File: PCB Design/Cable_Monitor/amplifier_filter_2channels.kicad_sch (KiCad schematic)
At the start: 6 parts, among them U2 MCP6002-xSN

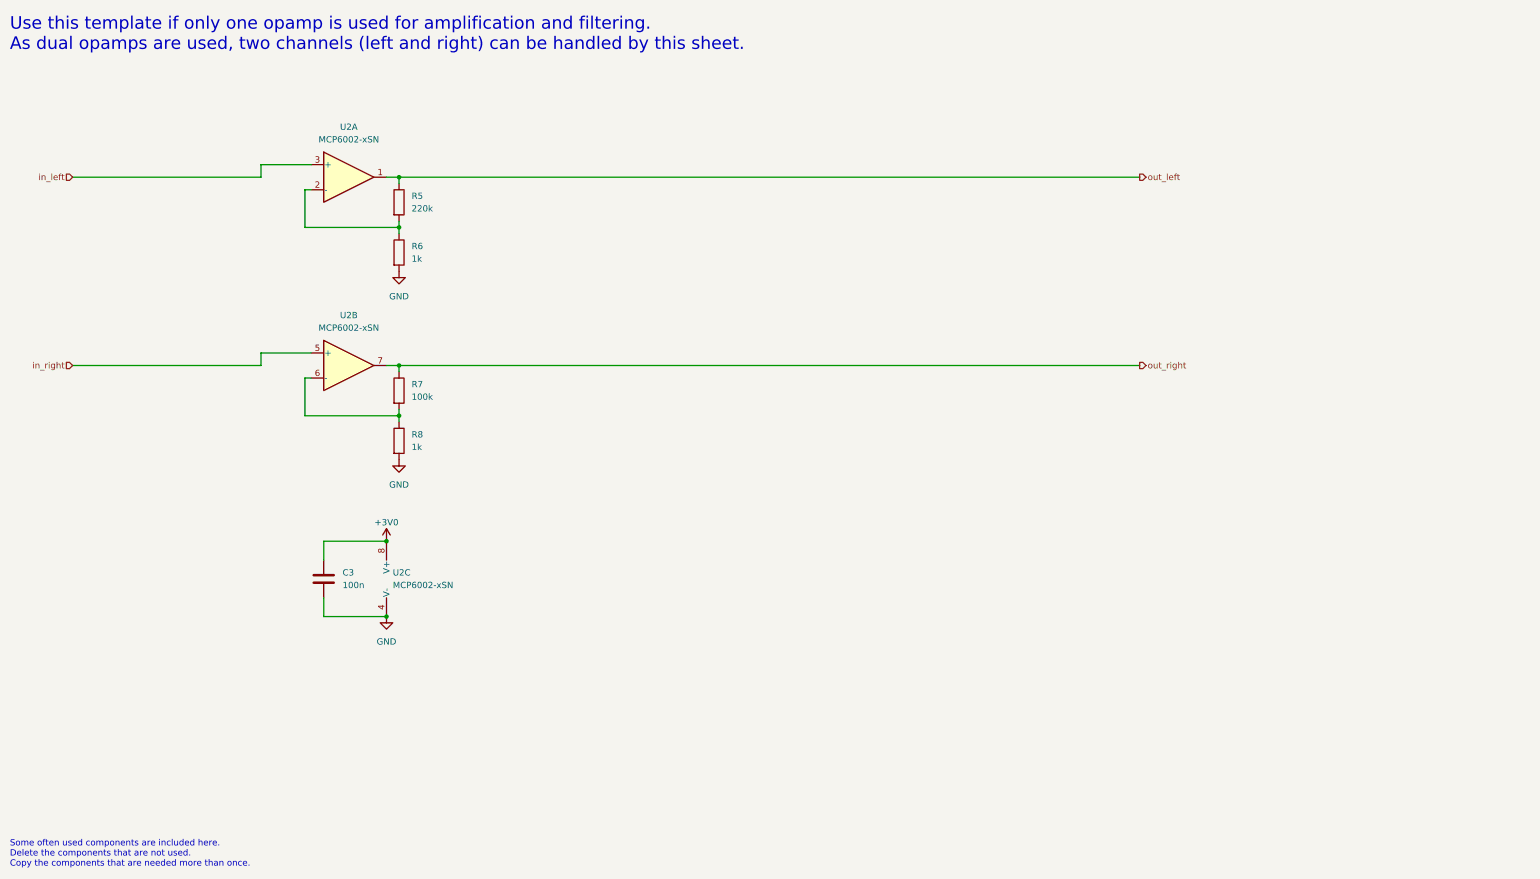
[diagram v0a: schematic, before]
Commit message: Modified Schematics
Added Virtual GND and adapted the Pads Left and Right
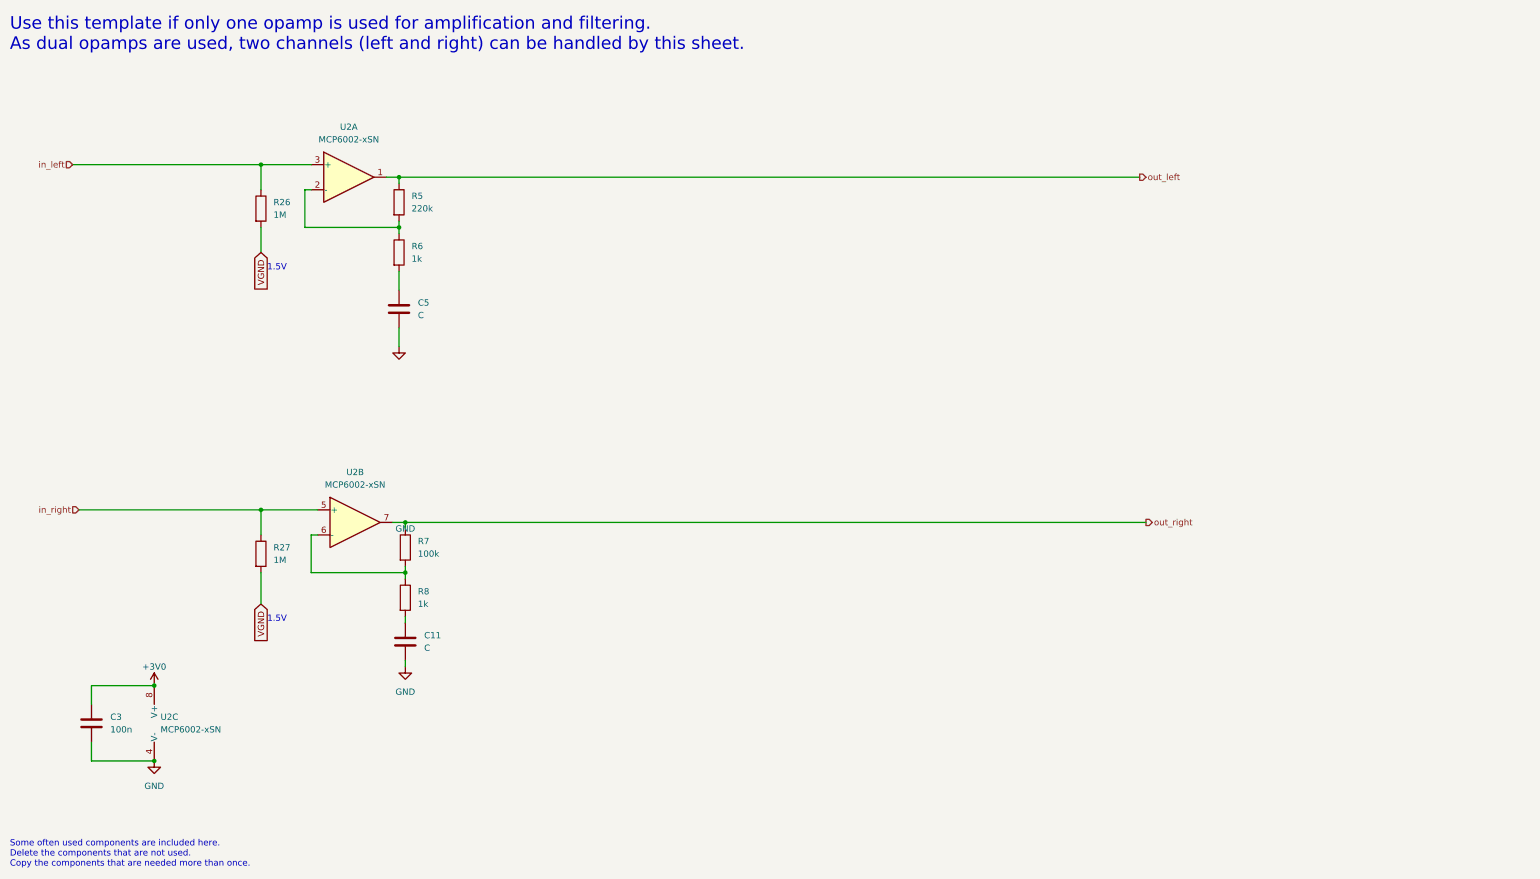
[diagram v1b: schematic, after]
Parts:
- added C11, C5: C, symbol Device:C
- added R26: 1M, Resistor_SMD:R_0805_2012Metric_Pad1.20x1.40mm_HandSolder, symbol Device:R
- added R27: 1M, symbol Device:R
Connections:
- net GND: now also C11.2, C5.2; no longer R6.2, R8.2
- net in_left: now also R26.1
- net in_right: now also R27.1
- new net: C11.1, R8.2
- new net: C5.1, R6.2
- new net VGND: R26.2, R27.2
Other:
- note added: "1.5V"
- moved on the sheet: C3, R7, R8, U2B, U2C

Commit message: PCB Layout Update
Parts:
- added C10, C11, C12, C13, C14, C15: C, symbol Device:C
- added C20: 100n, Capacitor_SMD:C_0805_2012Metric_Pad1.18x1.45mm_HandSolder, symbol Device:C
- added R10, R11, R12, R13, R14, R9: R, symbol Device:R
- added U3: MCP6002-xSN, Package_SO:SOIC-8_3.9x4.9mm_P1.27mm, symbol Amplifier_Operational:MCP6002-xSN
- renumbered C3 to C7, C5 to C8, C11 to C9, R26 to R3, R27 to R4, U2 to U4
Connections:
- net +3V0: now also C20.1, U3.4 (V-)
- net GND: now also C20.2, R11.2, R12.2, U3.8 (V+)
- net VGND: now also U3.3 (+), U3.5 (+)
- net out_left: now also C12.2, R13.1, U3.1; no longer R5.1, U4.1
- net out_right: now also C14.2, R14.1, U3.7; no longer R7.1, U4.7
- new net: C11.2, R10.1
- new net: C14.1, C15.1, R10.2, R12.1
- new net: C12.1, C13.1, R11.1, R9.2
- new net: C13.2, R13.2, U3.2 (-)
- new net: C11.1, R7.1, U4.7
- new net: C10.1, R5.1, U4.1
- new net: C15.2, R14.2, U3.6 (-)
- new net: C10.2, R9.1
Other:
- note added: "Supply Voltage for OPAmps"
- moved on the sheet: C7, C9, R4, R7, R8, U4B, U4C

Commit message: PCB Design Update
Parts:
- removed C10, C11, C8, C9: C, symbol Device:C
- removed R5: 220k, Resistor_SMD:R_0805_2012Metric_Pad1.20x1.40mm_HandSolder, symbol Device:R
- removed R7: 100k, Resistor_SMD:R_0805_2012Metric_Pad1.20x1.40mm_HandSolder, symbol Device:R
- removed R8: 1k, Resistor_SMD:R_0805_2012Metric_Pad1.20x1.40mm_HandSolder, symbol Device:R
- removed R9: R, symbol Device:R
- C11: renamed from C12; value C -> 18nF
- C12: renamed from C13; value C -> 330nF
- C13: renamed from C14; value C -> 18nF
- C14: renamed from C15; value C -> 330nF
- R10: renamed from R14; value R -> 560k
- R5: renamed from R10; value R -> 5.1k
- R6: value 1k -> 5.1k; footprint Resistor_SMD:R_0805_2012Metric_Pad1.20x1.40mm_HandSolder -> (none)
- R7: renamed from R11; value R -> 7.5k
- R8: renamed from R12; value R -> 7.5k
- R9: renamed from R13; value R -> 560k
- renumbered C20 to C10, C7 to C9, R4 to R3, R3 to R4, U4 to U5, U3 to U5, U3 to U6, U4 to U6
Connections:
- net VGND: now also U5.5 (+); no longer U5.3 (+)
- net in_right: now also U6.3 (+); no longer U6.5 (+)
- net out_left: now also U5.7; no longer U5.1
- net at R5.1: now also U6.1, U6.2 (-)
- net at C11.1, C12.1, R7.1: now also R6.2
- net at C12.2, R9.2: now also U5.6 (-); no longer U5.2 (-)
- net at U5.1: now also R6.1, U5.2 (-)
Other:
- moved on the sheet: R3, R4, R5

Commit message: Letzte Anpassungen am Schema
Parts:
- added TP4: pad_right_sf, TestPoint:TestPoint_Loop_D2.60mm_Drill1.6mm_Beaded, symbol Connector:TestPoint
- added TP4: pad_left_sf, TestPoint:TestPoint_Loop_D2.60mm_Drill1.6mm_Beaded, symbol Connector:TestPoint
- renumbered R7 to R10, R8 to R11, R9 to R12, R10 to R13, R3 to R6, R4 to R7, R5 to R8, R6 to R9
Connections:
- net at R8.1, U6.1, U6.2 (-): now also TP4.1
- net at R9.1, U5.1, U5.2 (-): now also TP4.1

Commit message: Schema Updates, bald Fertig
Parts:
- C11, C12, C13, C14: footprint (none) -> Capacitor_SMD:C_0805_2012Metric_Pad1.18x1.45mm_HandSolder
- R10, R11, R12, R13, R6, R8, R9: footprint (none) -> Resistor_SMD:R_0805_2012Metric_Pad1.20x1.40mm_HandSolder
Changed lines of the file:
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@@
       (effects (font (size 1.27 1.27)))
     )
-    (property "Footprint" "" (at 121.92 103.378 90)
+    (property "Footprint" "Resistor_SMD:R_0805_2012Metric_Pad1.20x1.40mm_HandSolder" (at 121.92 103.378 90)
       (effects (font (size 1.27 1.27)) hide)
     )
@@
       (effects (font (size 1.27 1.27)))
     )
-    (property "Footprint" "" (at 158.75 49.8348 0)
+    (property "Footprint" "Capacitor_SMD:C_0805_2012Metric_Pad1.18x1.45mm_HandSolder" (at 158.75 49.8348 0)
       (effects (font (size 1.27 1.27)) hide)
     )
@@
       (effects (font (size 1.27 1.27)) (justify left))
     )
-    (property "Footprint" "" (at 141.732 106.68 90)
+    (property "Footprint" "Resistor_SMD:R_0805_2012Metric_Pad1.20x1.40mm_HandSolder" (at 141.732 106.68 90)
       (effects (font (size 1.27 1.27)) hide)
     )
@@
       (effects (font (size 1.27 1.27)))
     )
-    (property "Footprint" "" (at 158.75 100.6348 0)
+    (property "Footprint" "Capacitor_SMD:C_0805_2012Metric_Pad1.18x1.45mm_HandSolder" (at 158.75 100.6348 0)
       (effects (font (size 1.27 1.27)) hide)
     )
@@
         )
         (path "/1f276d59-ad9b-4e70-a842-f3b7e562eb9b/12fcc65d-dd77-40b1-ae40-e29cdf7d08dc"
-          (reference "TP13") (unit 1)
+          (reference "TP20") (unit 1)
         )
       )
@@
       (effects (font (size 1.27 1.27)) (justify left))
     )
-    (property "Footprint" "" (at 160.782 95.25 90)
+    (property "Footprint" "Resistor_SMD:R_0805_2012Metric_Pad1.20x1.40mm_HandSolder" (at 160.782 95.25 90)
       (effects (font (size 1.27 1.27)) hide)
     )
@@
       (effects (font (size 1.27 1.27)) (justify left))
     )
-    (property "Footprint" "" (at 160.782 44.45 90)
+    (property "Footprint" "Resistor_SMD:R_0805_2012Metric_Pad1.20x1.40mm_HandSolder" (at 160.782 44.45 90)
       (effects (font (size 1.27 1.27)) hide)
     )
@@
       (effects (font (size 1.27 1.27)))
     )
-    (property "Footprint" "" (at 158.75 89.2048 0)
+    (property "Footprint" "Capacitor_SMD:C_0805_2012Metric_Pad1.18x1.45mm_HandSolder" (at 158.75 89.2048 0)
       (effects (font (size 1.27 1.27)) hide)
     )
@@
       (effects (font (size 1.27 1.27)))
     )
-    (property "Footprint" "" (at 123.19 52.578 90)
+    (property "Footprint" "Resistor_SMD:R_0805_2012Metric_Pad1.20x1.40mm_HandSolder" (at 123.19 52.578 90)
       (effects (font (size 1.27 1.27)) hide)
     )
@@
       (effects (font (size 1.27 1.27)) (justify left))
     )
-    (property "Footprint" "" (at 141.732 55.88 90)
+    (property "Footprint" "Resistor_SMD:R_0805_2012Metric_Pad1.20x1.40mm_HandSolder" (at 141.732 55.88 90)
       (effects (font (size 1.27 1.27)) hide)
     )
@@
       (effects (font (size 1.27 1.27)) (justify left))
     )
-    (property "Footprint" "" (at 73.152 113.03 90)
+    (property "Footprint" "Resistor_SMD:R_0805_2012Metric_Pad1.20x1.40mm_HandSolder" (at 73.152 113.03 90)
       (effects (font (size 1.27 1.27)) hide)
     )
@@
       (effects (font (size 1.27 1.27)))
     )
-    (property "Footprint" "" (at 158.75 38.4048 0)
+    (property "Footprint" "Capacitor_SMD:C_0805_2012Metric_Pad1.18x1.45mm_HandSolder" (at 158.75 38.4048 0)
       (effects (font (size 1.27 1.27)) hide)
     )
@@
         )
         (path "/1f276d59-ad9b-4e70-a842-f3b7e562eb9b/12fcc65d-dd77-40b1-ae40-e29cdf7d08dc"
-          (reference "TP12") (unit 1)
-        )
-      )
+          (reference "TP19") (unit 1)
+        )
+      )

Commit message: Update
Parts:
- renumbered R7 to R10, R8 to R11, R9 to R12, R10 to R13, R11 to R14, R12 to R15, R13 to R16, R6 to R9
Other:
- note added: "Filtering and Amplification to measure Electric Fields. This will allow us to measure Fields generated by Cables and thus allow us to calculate the distance from an AC Voltage source."
- note removed: "Some often used components are included here. Delete the components that are not used. Copy the components that are needed more than once."
- note removed: "Use this template if only one opamp is used for amplification and filtering. As dual opamps are used, two channels (left and right) can be handled by this sheet."
- company: hhrt@zhaw.ch -> ZHAW
- title: Amplifiers and Filters -> Amplifiers and Filters for Pads

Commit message: Almost Donezo
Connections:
- net +3V0: now also U6.8 (V+); no longer U6.4 (V-)
- net GND: now also U6.4 (V-); no longer U6.8 (V+)
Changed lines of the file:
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@@
     )
   )
-  (symbol (lib_id "Amplifier_Operational:MCP6002-xSN") (at 76.2 167.64 0) (mirror x) (unit 3)
+  (symbol (lib_id "Amplifier_Operational:MCP6002-xSN") (at 76.2 167.64 0) (unit 3)
     (in_bom yes) (on_board yes) (dnp no)
-    (property "Reference" "U6" (at 77.47 166.37 0)
+    (property "Reference" "U6" (at 77.47 168.91 0)
       (effects (font (size 1.27 1.27)))
     )
-    (property "Value" "MCP6002-xSN" (at 82.55 168.91 0)
+    (property "Value" "MCP6002-xSN" (at 82.55 166.37 0)
       (effects (font (size 1.27 1.27)))
     )
@@
       (effects (font (size 1.27 1.27)) hide)
     )
-    (property "Sim.Pins" "1=1out 2=1in- 3=1in+ 4=vcc- 5=2in+ 6=2in- 7=2out 8=vcc+" (at -17.78 218.44 0)
+    (property "Sim.Pins" "1=1out 2=1in- 3=1in+ 4=vcc- 5=2in+ 6=2in- 7=2out 8=vcc+" (at -17.78 116.84 0)
       (effects (font (size 1.27 1.27)) hide)
     )

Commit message: Updated Schematics
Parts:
- renumbered C9 to C10, C10 to C11, C11 to C12, C12 to C13, C13 to C14, C14 to C15
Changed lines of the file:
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@@
   (symbol (lib_id "Device:C") (at 154.94 50.8 90) (unit 1)
     (in_bom yes) (on_board yes) (dnp no)
-    (property "Reference" "C12" (at 154.94 54.61 90)
+    (property "Reference" "C13" (at 154.94 54.61 90)
       (effects (font (size 1.27 1.27)))
     )
@@
       (project "Cable_Monitor"
         (path "/1f276d59-ad9b-4e70-a842-f3b7e562eb9b/12fcc65d-dd77-40b1-ae40-e29cdf7d08dc"
-          (reference "C12") (unit 1)
+          (reference "C13") (unit 1)
         )
       )
@@
   (symbol (lib_id "power:GND") (at 73.66 175.26 0) (unit 1)
     (in_bom yes) (on_board yes) (dnp no) (fields_autoplaced)
-    (property "Reference" "#PWR039" (at 73.66 181.61 0)
+    (property "Reference" "#PWR040" (at 73.66 181.61 0)
       (effects (font (size 1.27 1.27)) hide)
     )
@@
       (project "Cable_Monitor"
         (path "/1f276d59-ad9b-4e70-a842-f3b7e562eb9b/12fcc65d-dd77-40b1-ae40-e29cdf7d08dc"
-          (reference "#PWR039") (unit 1)
+          (reference "#PWR040") (unit 1)
         )
       )
@@
   (symbol (lib_id "power:GND") (at 40.64 175.26 0) (unit 1)
     (in_bom yes) (on_board yes) (dnp no) (fields_autoplaced)
-    (property "Reference" "#PWR037" (at 40.64 181.61 0)
+    (property "Reference" "#PWR038" (at 40.64 181.61 0)
       (effects (font (size 1.27 1.27)) hide)
     )
@@
       (project "Cable_Monitor"
         (path "/1f276d59-ad9b-4e70-a842-f3b7e562eb9b/12fcc65d-dd77-40b1-ae40-e29cdf7d08dc"
-          (reference "#PWR037") (unit 1)
+          (reference "#PWR038") (unit 1)
         )
       )
@@
   (symbol (lib_id "Device:C") (at 60.96 167.64 0) (unit 1)
     (in_bom yes) (on_board yes) (dnp no)
-    (property "Reference" "C10" (at 64.77 166.3699 0)
+    (property "Reference" "C11" (at 64.77 166.3699 0)
       (effects (font (size 1.27 1.27)) (justify left))
     )
@@
       (project "Cable_Monitor"
         (path "/1f276d59-ad9b-4e70-a842-f3b7e562eb9b/12fcc65d-dd77-40b1-ae40-e29cdf7d08dc"
-          (reference "C10") (unit 1)
+          (reference "C11") (unit 1)
         )
       )
@@
   (symbol (lib_id "power:GND") (at 143.51 63.5 0) (unit 1)
     (in_bom yes) (on_board yes) (dnp no) (fields_autoplaced)
-    (property "Reference" "#PWR040" (at 143.51 69.85 0)
+    (property "Reference" "#PWR041" (at 143.51 69.85 0)
       (effects (font (size 1.27 1.27)) hide)
     )
@@
       (project "Cable_Monitor"
         (path "/1f276d59-ad9b-4e70-a842-f3b7e562eb9b/12fcc65d-dd77-40b1-ae40-e29cdf7d08dc"
-          (reference "#PWR040") (unit 1)
+          (reference "#PWR041") (unit 1)
         )
       )
@@
   (symbol (lib_id "Device:C") (at 154.94 101.6 90) (unit 1)
     (in_bom yes) (on_board yes) (dnp no)
-    (property "Reference" "C14" (at 154.94 105.41 90)
+    (property "Reference" "C15" (at 154.94 105.41 90)
       (effects (font (size 1.27 1.27)))
     )
@@
       (project "Cable_Monitor"
         (path "/1f276d59-ad9b-4e70-a842-f3b7e562eb9b/12fcc65d-dd77-40b1-ae40-e29cdf7d08dc"
-          (reference "C14") (unit 1)
+          (reference "C15") (unit 1)
         )
       )
@@
   (symbol (lib_id "power:+3V0") (at 40.64 160.02 0) (unit 1)
     (in_bom yes) (on_board yes) (dnp no)
-    (property "Reference" "#PWR036" (at 40.64 163.83 0)
+    (property "Reference" "#PWR037" (at 40.64 163.83 0)
       (effects (font (size 1.27 1.27)) hide)
     )
@@
       (project "Cable_Monitor"
         (path "/1f276d59-ad9b-4e70-a842-f3b7e562eb9b/12fcc65d-dd77-40b1-ae40-e29cdf7d08dc"
-          (reference "#PWR036") (unit 1)
+          (reference "#PWR037") (unit 1)
         )
       )
@@
   (symbol (lib_id "power:+3V0") (at 73.66 160.02 0) (unit 1)
     (in_bom yes) (on_board yes) (dnp no)
-    (property "Reference" "#PWR038" (at 73.66 163.83 0)
+    (property "Reference" "#PWR039" (at 73.66 163.83 0)
       (effects (font (size 1.27 1.27)) hide)
     )
@@
       (project "Cable_Monitor"
         (path "/1f276d59-ad9b-4e70-a842-f3b7e562eb9b/12fcc65d-dd77-40b1-ae40-e29cdf7d08dc"
-          (reference "#PWR038") (unit 1)
+          (reference "#PWR039") (unit 1)
         )
       )
@@
   (symbol (lib_id "Device:C") (at 154.94 90.17 90) (unit 1)
     (in_bom yes) (on_board yes) (dnp no)
-    (property "Reference" "C13" (at 154.94 83.82 90)
+    (property "Reference" "C14" (at 154.94 83.82 90)
       (effects (font (size 1.27 1.27)))
     )
@@
       (project "Cable_Monitor"
         (path "/1f276d59-ad9b-4e70-a842-f3b7e562eb9b/12fcc65d-dd77-40b1-ae40-e29cdf7d08dc"
-          (reference "C13") (unit 1)
+          (reference "C14") (unit 1)
         )
       )
@@
   (symbol (lib_id "Device:C") (at 27.94 167.64 0) (unit 1)
     (in_bom yes) (on_board yes) (dnp no) (fields_autoplaced)
-    (property "Reference" "C9" (at 31.75 166.3699 0)
+    (property "Reference" "C10" (at 31.75 166.3699 0)
       (effects (font (size 1.27 1.27)) (justify left))
     )
@@
       (project "Cable_Monitor"
         (path "/1f276d59-ad9b-4e70-a842-f3b7e562eb9b/12fcc65d-dd77-40b1-ae40-e29cdf7d08dc"
-          (reference "C9") (unit 1)
+          (reference "C10") (unit 1)
         )
       )
@@
   (symbol (lib_id "Device:C") (at 154.94 39.37 90) (unit 1)
     (in_bom yes) (on_board yes) (dnp no)
-    (property "Reference" "C11" (at 154.94 33.02 90)
+    (property "Reference" "C12" (at 154.94 33.02 90)
       (effects (font (size 1.27 1.27)))
     )
@@
       (project "Cable_Monitor"
         (path "/1f276d59-ad9b-4e70-a842-f3b7e562eb9b/12fcc65d-dd77-40b1-ae40-e29cdf7d08dc"
-          (reference "C11") (unit 1)
+          (reference "C12") (unit 1)
         )
       )
@@
   (symbol (lib_id "power:GND") (at 143.51 114.3 0) (unit 1)
     (in_bom yes) (on_board yes) (dnp no) (fields_autoplaced)
-    (property "Reference" "#PWR041" (at 143.51 120.65 0)
+    (property "Reference" "#PWR042" (at 143.51 120.65 0)
       (effects (font (size 1.27 1.27)) hide)
     )
@@
       (project "Cable_Monitor"
         (path "/1f276d59-ad9b-4e70-a842-f3b7e562eb9b/12fcc65d-dd77-40b1-ae40-e29cdf7d08dc"
-          (reference "#PWR041") (unit 1)
-        )
-      )
+          (reference "#PWR042") (unit 1)
+        )
+      )
